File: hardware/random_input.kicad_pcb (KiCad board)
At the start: 2 copper layers, 34 x 32.4 mm, 17 parts, among them J1 E1, Q1 NPN Ge, Q2 NPN Ge

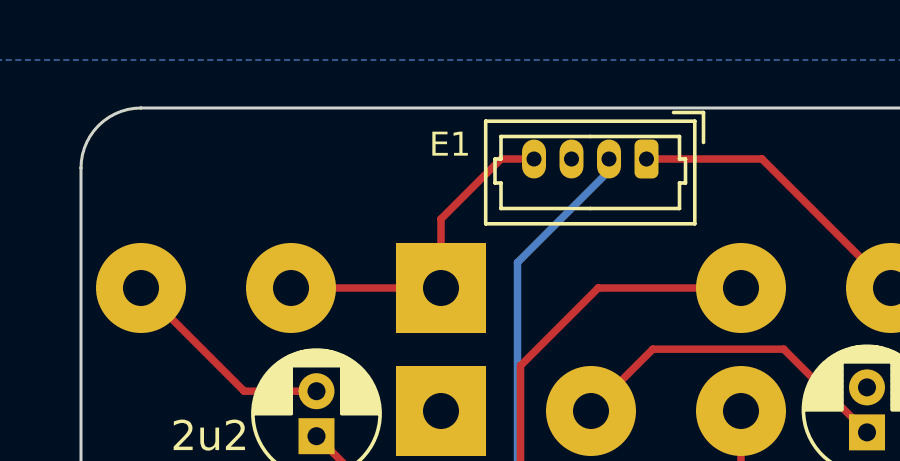
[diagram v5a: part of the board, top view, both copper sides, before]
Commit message: Some updates based on feedback from freestompboxes.org folks:
 - Add back thermal reliefs on ground pads
 - Add 3D models for various parts (courtesy of Vasily Kashirin - https://grabcad.com/vasily.kashirin-1/models?page=1)
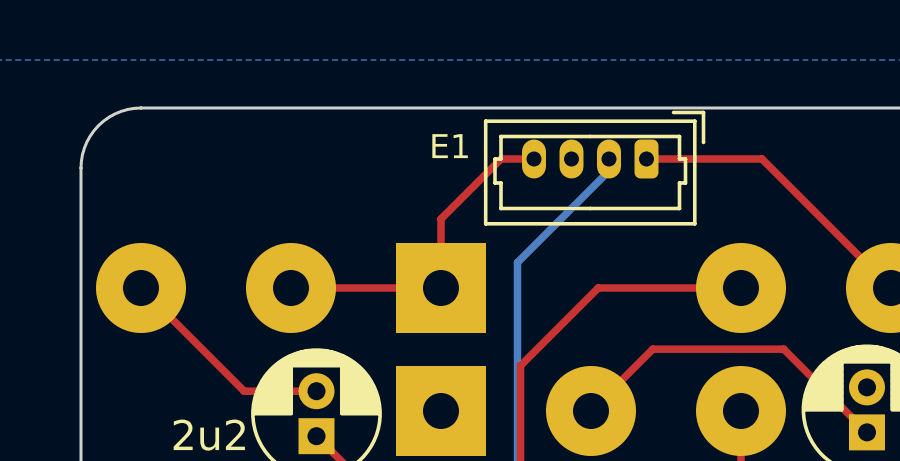
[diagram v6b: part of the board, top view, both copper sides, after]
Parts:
- J1: footprint Connector_Molex:Molex_PicoBlade_53047-0410_1x04_P1.25mm_Vertical -> random_input:Molex_PicoBlade_53047-0410_1x04_P1.25mm_Vertical_with_3D_Model
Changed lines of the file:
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@@
   (title_block
     (title "Random Input Fuzz Effect")
-    (date "2023-03-03")
-    (rev "v0.26")
+    (date "2023-03-04")
+    (rev "v0.27")
     (comment 1 "github.com/whbeers/random_input")
   )
@@
     )
   )
-  (footprint "Connector_Molex:Molex_PicoBlade_53047-0410_1x04_P1.25mm_Vertical" (layer "F.Cu")
+  (footprint "random_input:Molex_PicoBlade_53047-0410_1x04_P1.25mm_Vertical_with_3D_Model" (layer "F.Cu")
     (at 48.85 25.8 180)
     (descr "Molex PicoBlade Connector System, 53047-0410, 4 Pins per row (http://www.molex.com/pdm_docs/sd/530470610_sd.pdf), generated with kicad-footprint-generator")
@@
     (property "ki_keywords" "connector")
     (attr through_hole)
-    (fp_text reference "J1" (at 1.88 -3.25) (layer "F.Fab")
-        (effects (font (size 1 1) (thickness 0.15)))
-    )
-    (fp_text value "E1" (at 1.88 2.35) (layer "F.Fab")
-        (effects (font (size 1 1) (thickness 0.15)))
-    )
-    (fp_text user "E1" (at 6.55 0.95 unlocked) (layer "F.SilkS" knockout)
-        (effects (font (size 0.8 0.8) (thickness 0.15)) (justify top))
-    )
-    (fp_text user "${REFERENCE}" (at 1.88 -1.35) (layer "F.Fab")
+    (fp_text reference "J1" (at 1.88 -3.25 180) (layer "F.Fab")
+        (effects (font (size 1 1) (thickness 0.15)))
+    )
+    (fp_text value "E1" (at 6.55 0.4 180) (layer "F.SilkS" knockout)
+        (effects (font (size 0.8 0.8) (thickness 0.15)))
+    )
+    (fp_text user "${REFERENCE}" (at 1.88 -1.35 180) (layer "F.Fab")
         (effects (font (size 1 1) (thickness 0.15)))
     )
@@
       (scale (xyz 1 1 1))
       (rotate (xyz 0 0 0))
+    )
+    (model "/home/whbeers/src-mine/stepfiles/530470410.stp"
+      (offset (xyz 1.9 -1.15 5.5))
+      (scale (xyz 1 1 1))
+      (rotate (xyz 90 0 0))
     )
   )
@@
     (pad "3" thru_hole circle (at 4.9925 -3.81 90) (size 3 3) (drill 1.2) (layers "*.Cu" "*.Mask")
       (net 10 "/Q2_E") (pinfunction "3") (pintype "passive"))
+    (model "/home/whbeers/src-mine/stepfiles/RV16AF-41.step"
+      (offset (xyz 0 12.2 0.5))
+      (scale (xyz 1 1 1))
+      (rotate (xyz 0 0 0))
+    )
   )
   (footprint "random_input:Potentiometer_Single_3_Horizontal" (layer "B.Cu")
@@
     (pad "3" thru_hole circle (at 4.9925 -3.81 270) (size 3 3) (drill 1.2) (layers "*.Cu" "*.Mask")
       (net 9 "/PRE_VOLUME") (pinfunction "3") (pintype "passive"))
+    (model "/home/whbeers/src-mine/stepfiles/RV16AF-41.step"
+      (offset (xyz 0 12.2 0.5))
+      (scale (xyz 1 1 1))
+      (rotate (xyz 0 0 0))
+    )
   )
   (footprint "random_input:Potentiometer_Single_3_Horizontal" (layer "B.Cu")
@@
     (pad "3" thru_hole circle (at 4.9925 -3.81 270) (size 3 3) (drill 1.2) (layers "*.Cu" "*.Mask")
       (net 2 "Net-(C2-Pad2)") (pinfunction "3") (pintype "passive"))
+    (model "/home/whbeers/src-mine/stepfiles/RV16AF-41.step"
+      (offset (xyz 0 12.2 0.5))
+      (scale (xyz 1 1 1))
+      (rotate (xyz 0 0 0))
+    )
   )
   (gr_line (start 30 54.5) (end 30 26.1)
@@
   (segment (start 60.92 49.1) (end 59.82 50.2) (width 0.25) (layer "F.Cu") (net 12))
   (zone (net 1) (net_name "GND") (layer "B.Cu") (hatch edge 0.5)
-    (connect_pads yes (clearance 0.5))
+    (connect_pads thru_hole_only (clearance 0.5))
     (min_thickness 0.25) (filled_areas_thickness no)
     (fill yes (thermal_gap 0.5) (thermal_bridge_width 0.5))
